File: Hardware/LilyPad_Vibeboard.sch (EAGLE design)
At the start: 10 parts, among them M1 MOTORSMD

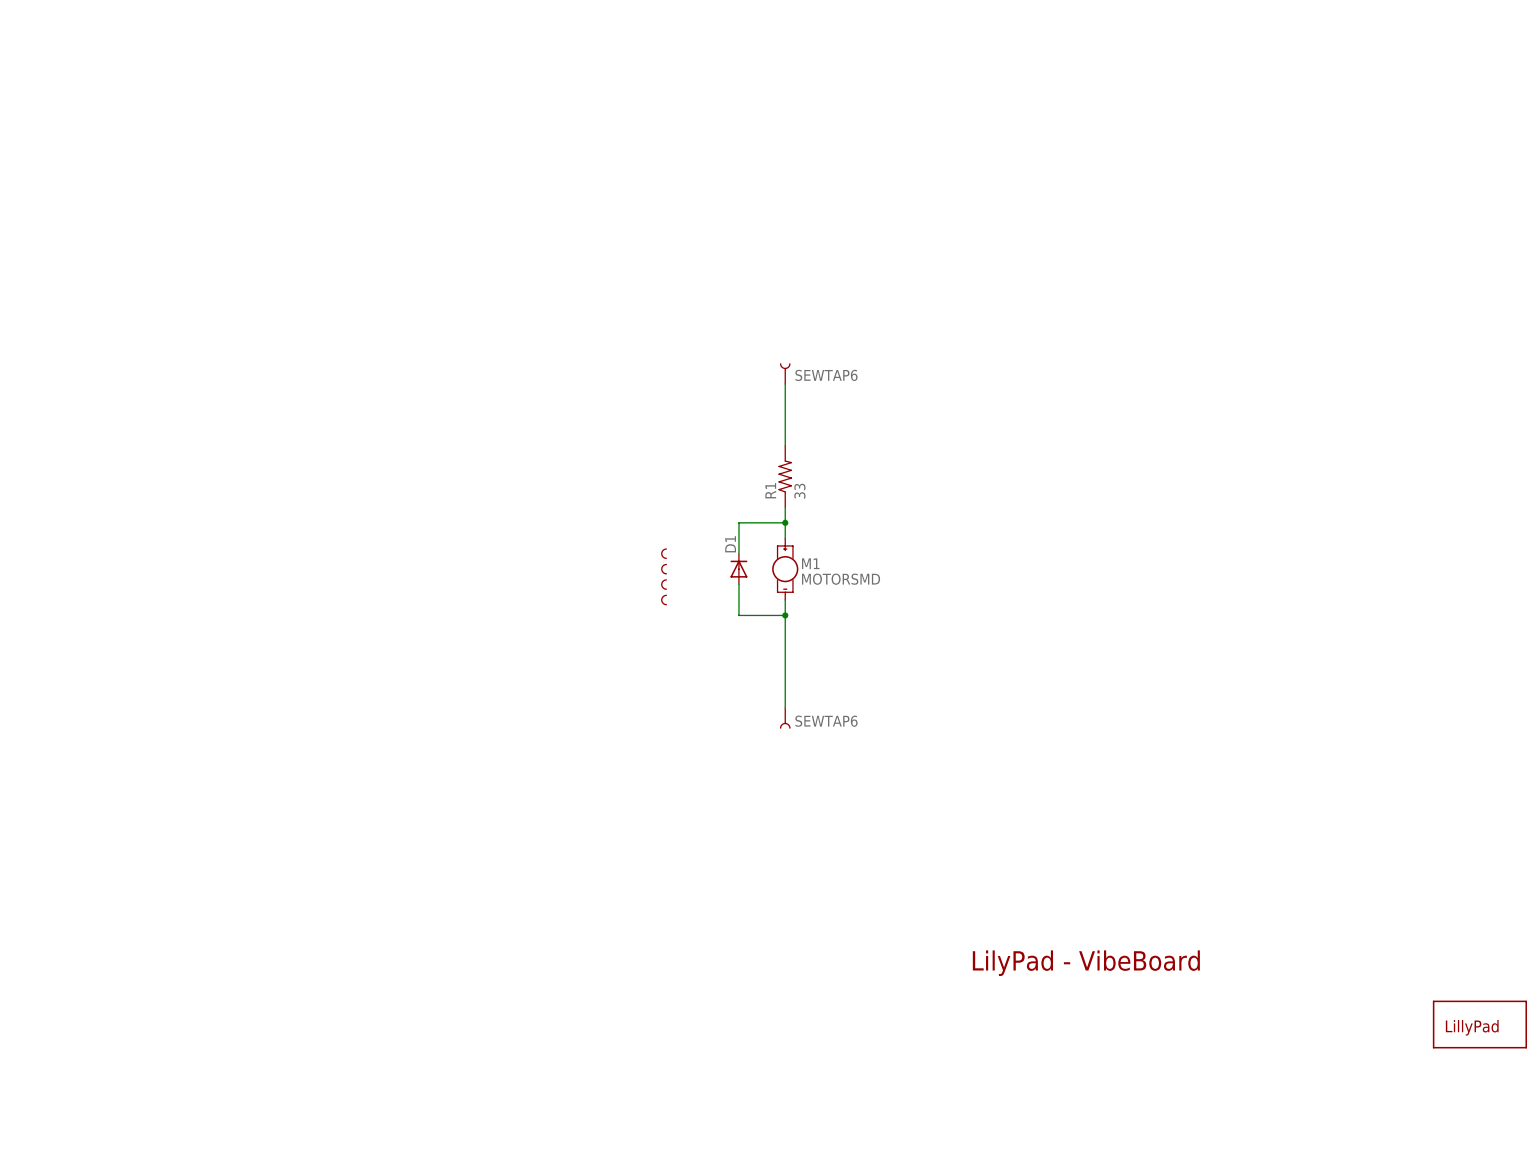
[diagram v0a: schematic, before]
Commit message: Updated Schematic, Trace Routing added OSHW logo
Updated schematic to "frame letter"  re-routed previous traces that did
not pass the angle check, added OSHW logo.
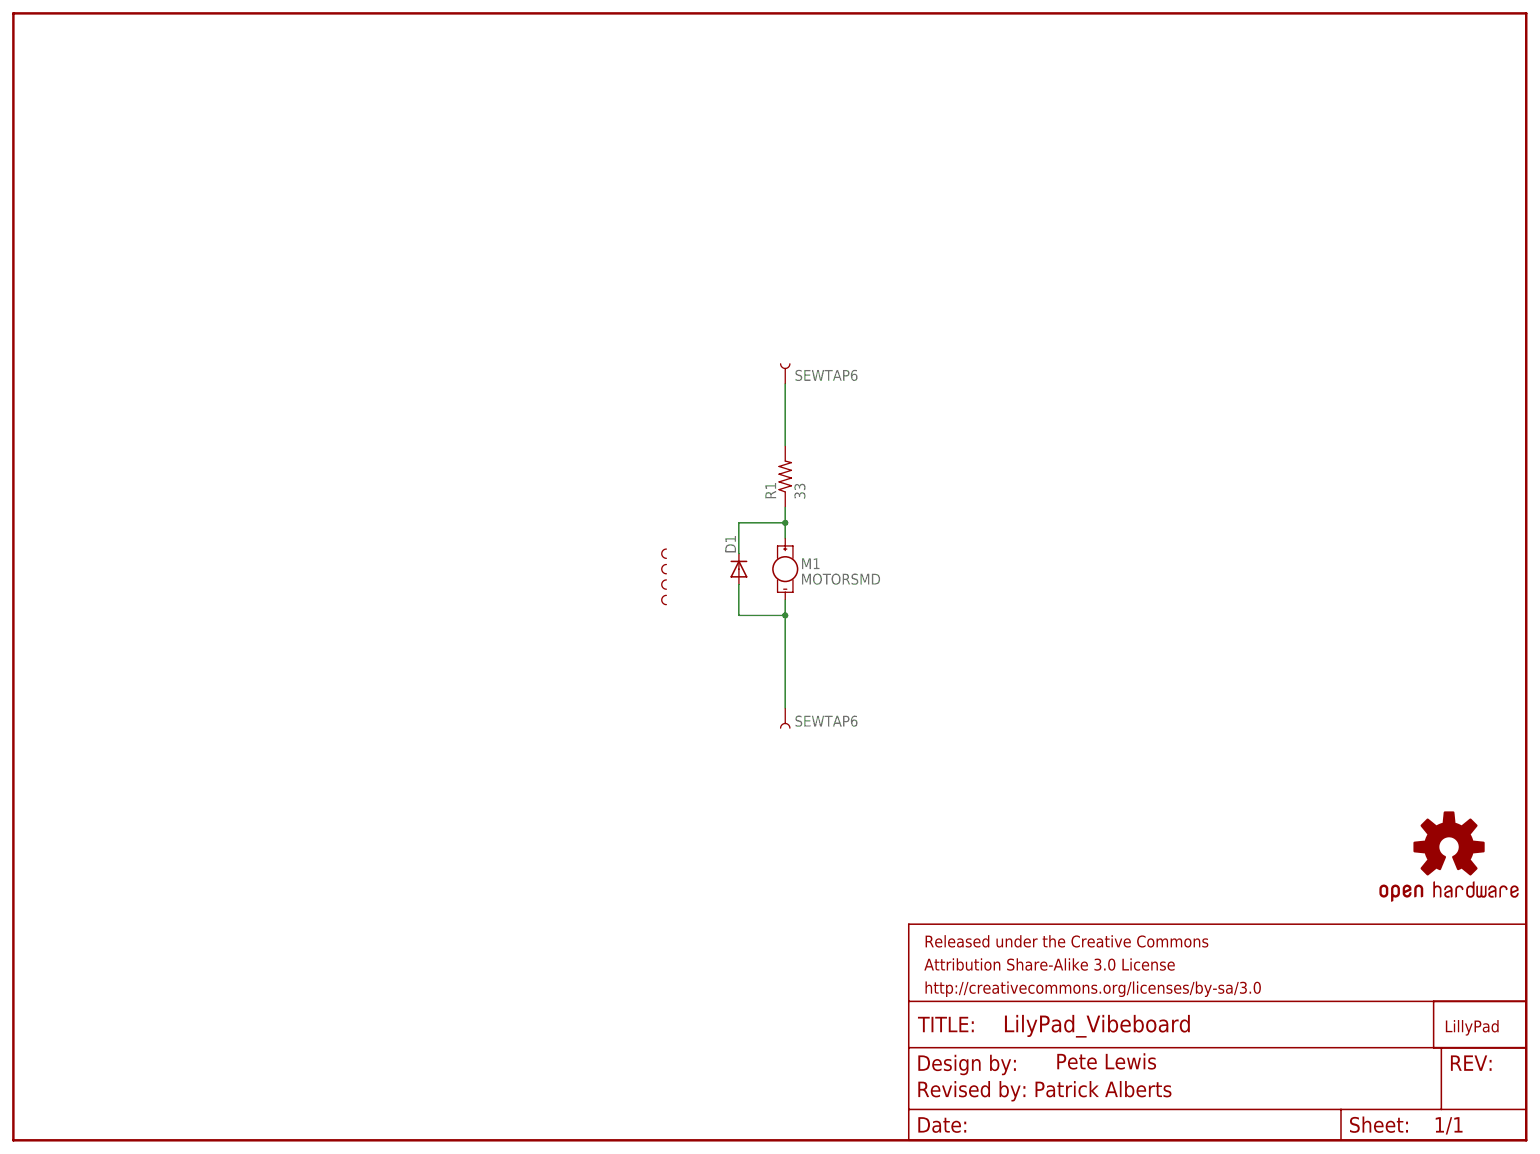
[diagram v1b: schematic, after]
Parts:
- added FRAME1: FRAME-LETTER, SparkFun-Aesthetics:FRAME-LETTER
- added LOGO1: OSHW-LOGOS, SparkFun-Aesthetics:OSHW-LOGOS
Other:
- note added: "Pete Lewis"
- note added: "Revised by: Patrick Alberts"
- note removed: "LilyPad - VibeBoard"
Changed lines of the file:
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@@
 <layer number="144" name="Drill_legend" color="7" fill="1" visible="yes" active="yes"/>
 <layer number="151" name="HeatSink" color="7" fill="1" visible="yes" active="yes"/>
+<layer number="199" name="Contour" color="7" fill="1" visible="no" active="yes"/>
 <layer number="200" name="200bmp" color="1" fill="10" visible="no" active="no"/>
 <layer number="201" name="201bmp" color="2" fill="1" visible="no" active="no"/>
@@
 </classes>
 <parts>
-<part name="FRAME1" library="SparkFun" deviceset="FRAME-LETTER" device=""/>
+<part name="FRAME1" library="SparkFun-Aesthetics" deviceset="FRAME-LETTER" device=""/>
 <part name="VIBE3" library="LilyPad-Wearables" deviceset="SEWTAP-NOHOLE" device="2"/>
 <part name="VIBE2" library="Testing" deviceset="SEWTAP-NOHOLE" device="W-MASK"/>
@@
 <part name="U$2" library="LilyPad-Wearables" deviceset="LOGO-LP" device="LP"/>
 <part name="R1" library="SparkFun-Resistors" deviceset="33K-1%" device="" value="33"/>
+<part name="LOGO1" library="SparkFun-Aesthetics" deviceset="OSHW-LOGO" device="S"/>
 </parts>
 <sheets>
 <sheet>
 <plain>
-<text x="157.48" y="27.94" size="3.175" layer="94">LilyPad - VibeBoard</text>
+<text x="171.45" y="11.684" size="2.54" layer="94" font="vector">Pete Lewis</text>
+<text x="148.59" y="7.112" size="2.54" layer="94" font="vector">Revised by: Patrick Alberts</text>
 </plain>
 <instances>
@@
 <instance part="U$2" gate="G$1" x="236.22" y="17.78"/>
 <instance part="R1" gate="G$1" x="127" y="109.22" rot="R90"/>
+<instance part="LOGO1" gate="G$1" x="236.22" y="48.26"/>
 </instances>
 <busses>

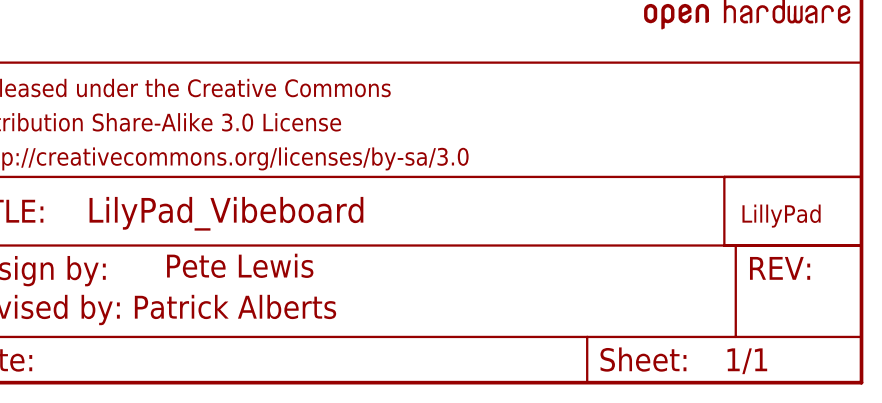
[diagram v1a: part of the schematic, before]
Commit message: Changed Silk
Moved posi/neg silk marks so that they can be clearly seen.
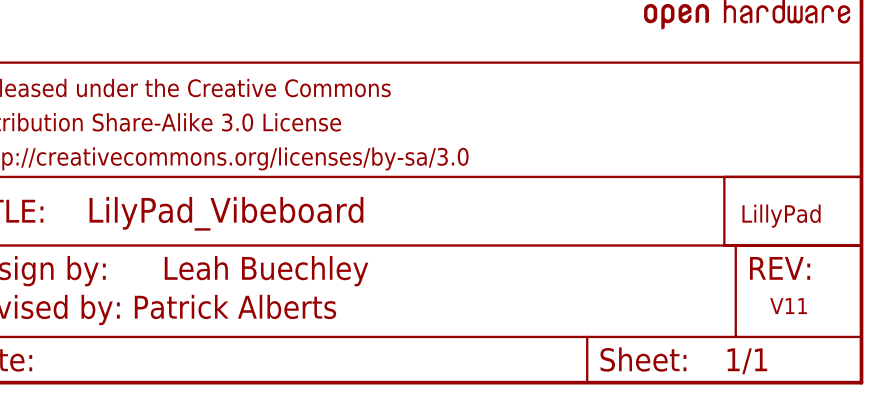
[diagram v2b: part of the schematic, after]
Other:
- note added: "Leah Buechley"
- note added: "V11"
- note removed: "Pete Lewis"
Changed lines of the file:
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@@
 <sheet>
 <plain>
-<text x="171.45" y="11.684" size="2.54" layer="94" font="vector">Pete Lewis</text>
 <text x="148.59" y="7.112" size="2.54" layer="94" font="vector">Revised by: Patrick Alberts</text>
+<text x="171.196" y="11.43" size="2.54" layer="94" font="vector">Leah Buechley</text>
+<text x="238.76" y="7.62" size="1.778" layer="94">V11</text>
 </plain>
 <instances>
